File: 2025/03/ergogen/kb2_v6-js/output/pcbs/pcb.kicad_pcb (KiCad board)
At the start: 2 copper layers, 256 x 72 mm, 66 parts

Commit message: finish? keyboard
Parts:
- added _10: , Mount_Hole_2.2mm_Pad_Via, F.Cu at (235.0, 117.0)
- added _11: , Mount_Hole_2.2mm_Pad_Via, F.Cu at (181.0, 135.7)
- added _12: , Mount_Hole_2.2mm_Pad_Via, F.Cu at (253.0, 135.7)
- added _9: , Mount_Hole_2.2mm_Pad_Via, F.Cu at (254.0, 106.8)
- moved _4 145.8 mm to (180.0, 106.8)
- moved _3 72.8 mm to (180.5, 84.7)
- moved _6 68.0 mm to (325.0, 91.5)
- moved _8 55.5 mm to (252.5, 84.7)
- moved _7 50.9 mm to (235.0, 91.5)
- moved _5 27.0 mm to (199.0, 117.0)
- moved _2 18.0 mm to (199.0, 91.5)
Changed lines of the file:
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@@
         )
         (module "Mount_Hole_2.2mm_Pad_Via" (layer "F.Cu")
-          (at 181 91.5 0)
+          (at 199 91.5 0)
           (fp_text reference "_2" (at 0 -3.2) (layer "F.SilkS") hide
             (effects (font (size 1 1) (thickness 0.15)))
@@
         )
         (module "Mount_Hole_2.2mm_Pad_Via" (layer "F.Cu")
-          (at 253 91.5 0)
+          (at 180.5 84.7 0)
           (fp_text reference "_3" (at 0 -3.2) (layer "F.SilkS") hide
             (effects (font (size 1 1) (thickness 0.15)))
@@
         )
         (module "Mount_Hole_2.2mm_Pad_Via" (layer "F.Cu")
-          (at 325 91.5 0)
+          (at 180 106.8 0)
           (fp_text reference "_4" (at 0 -3.2) (layer "F.SilkS") hide
             (effects (font (size 1 1) (thickness 0.15)))
@@
         )
         (module "Mount_Hole_2.2mm_Pad_Via" (layer "F.Cu")
-          (at 172 117 0)
+          (at 199 117 0)
           (fp_text reference "_5" (at 0 -3.2) (layer "F.SilkS") hide
             (effects (font (size 1 1) (thickness 0.15)))
@@
         )
         (module "Mount_Hole_2.2mm_Pad_Via" (layer "F.Cu")
-          (at 262 117 0)
+          (at 325 91.5 0)
           (fp_text reference "_6" (at 0 -3.2) (layer "F.SilkS") hide
             (effects (font (size 1 1) (thickness 0.15)))
@@
         )
         (module "Mount_Hole_2.2mm_Pad_Via" (layer "F.Cu")
-          (at 207 134 0)
+          (at 235 91.5 0)
           (fp_text reference "_7" (at 0 -3.2) (layer "F.SilkS") hide
             (effects (font (size 1 1) (thickness 0.15)))
@@
         )
         (module "Mount_Hole_2.2mm_Pad_Via" (layer "F.Cu")
-          (at 227 134 0)
+          (at 252.5 84.7 0)
           (fp_text reference "_8" (at 0 -3.2) (layer "F.SilkS") hide
             (effects (font (size 1 1) (thickness 0.15)))
           )
+          (fp_circle (center 0 0) (end 2.45 0) (layer "F.CrtYd") (width 0.05) (fill none))
+          (pad "1" thru_hole circle locked (at 0 0) (size 4.4 4.4) (drill 2.2) (layers *.Cu *.Mask))
+          (pad "1" thru_hole circle locked (at 1.6296296296296298 0) (size 0.7 0.7) (drill 0.4) (layers *.Cu *.Mask))
+(pad "1" thru_hole circle locked (at 1.1523221619336332 1.152322161933633) (size 0.7 0.7) (drill 0.4) (layers *.Cu *.Mask))
+(pad "1" thru_hole circle locked (at 9.978603548608063e-17 1.6296296296296298) (size 0.7 0.7) (drill 0.4) (layers *.Cu *.Mask))
+(pad "1" thru_hole circle locked (at -1.152322161933633 1.1523221619336332) (size 0.7 0.7) (drill 0.4) (layers *.Cu *.Mask))
+(pad "1" thru_hole circle locked (at -1.6296296296296298 1.9957207097216127e-16) (size 0.7 0.7) (drill 0.4) (layers *.Cu *.Mask))
+(pad "1" thru_hole circle locked (at -1.1523221619336335 -1.152322161933633) (size 0.7 0.7) (drill 0.4) (layers *.Cu *.Mask))
+(pad "1" thru_hole circle locked (at -2.993581064582419e-16 -1.6296296296296298) (size 0.7 0.7) (drill 0.4) (layers *.Cu *.Mask))
+(pad "1" thru_hole circle locked (at 1.1523221619336328 -1.1523221619336335) (size 0.7 0.7) (drill 0.4) (layers *.Cu *.Mask))
+        )
+        (module "Mount_Hole_2.2mm_Pad_Via" (layer "F.Cu")
+          (at 254 106.8 0)
+          (fp_text reference "_9" (at 0 -3.2) (layer "F.SilkS") hide
+            (effects (font (size 1 1) (thickness 0.15)))
+          )
+          (fp_circle (center 0 0) (end 2.45 0) (layer "F.CrtYd") (width 0.05) (fill none))
+          (pad "1" thru_hole circle locked (at 0 0) (size 4.4 4.4) (drill 2.2) (layers *.Cu *.Mask))
+          (pad "1" thru_hole circle locked (at 1.6296296296296298 0) (size 0.7 0.7) (drill 0.4) (layers *.Cu *.Mask))
+(pad "1" thru_hole circle locked (at 1.1523221619336332 1.152322161933633) (size 0.7 0.7) (drill 0.4) (layers *.Cu *.Mask))
+(pad "1" thru_hole circle locked (at 9.978603548608063e-17 1.6296296296296298) (size 0.7 0.7) (drill 0.4) (layers *.Cu *.Mask))
+(pad "1" thru_hole circle locked (at -1.152322161933633 1.1523221619336332) (size 0.7 0.7) (drill 0.4) (layers *.Cu *.Mask))
+(pad "1" thru_hole circle locked (at -1.6296296296296298 1.9957207097216127e-16) (size 0.7 0.7) (drill 0.4) (layers *.Cu *.Mask))
+(pad "1" thru_hole circle locked (at -1.1523221619336335 -1.152322161933633) (size 0.7 0.7) (drill 0.4) (layers *.Cu *.Mask))
+(pad "1" thru_hole circle locked (at -2.993581064582419e-16 -1.6296296296296298) (size 0.7 0.7) (drill 0.4) (layers *.Cu *.Mask))
+(pad "1" thru_hole circle locked (at 1.1523221619336328 -1.1523221619336335) (size 0.7 0.7) (drill 0.4) (layers *.Cu *.Mask))
+        )
+        (module "Mount_Hole_2.2mm_Pad_Via" (layer "F.Cu")
+          (at 235 117 0)
+          (fp_text reference "_10" (at 0 -3.2) (layer "F.SilkS") hide
+            (effects (font (size 1 1) (thickness 0.15)))
+          )
+          (fp_circle (center 0 0) (end 2.45 0) (layer "F.CrtYd") (width 0.05) (fill none))
+          (pad "1" thru_hole circle locked (at 0 0) (size 4.4 4.4) (drill 2.2) (layers *.Cu *.Mask))
+          (pad "1" thru_hole circle locked (at 1.6296296296296298 0) (size 0.7 0.7) (drill 0.4) (layers *.Cu *.Mask))
+(pad "1" thru_hole circle locked (at 1.1523221619336332 1.152322161933633) (size 0.7 0.7) (drill 0.4) (layers *.Cu *.Mask))
+(pad "1" thru_hole circle locked (at 9.978603548608063e-17 1.6296296296296298) (size 0.7 0.7) (drill 0.4) (layers *.Cu *.Mask))
+(pad "1" thru_hole circle locked (at -1.152322161933633 1.1523221619336332) (size 0.7 0.7) (drill 0.4) (layers *.Cu *.Mask))
+(pad "1" thru_hole circle locked (at -1.6296296296296298 1.9957207097216127e-16) (size 0.7 0.7) (drill 0.4) (layers *.Cu *.Mask))
+(pad "1" thru_hole circle locked (at -1.1523221619336335 -1.152322161933633) (size 0.7 0.7) (drill 0.4) (layers *.Cu *.Mask))
+(pad "1" thru_hole circle locked (at -2.993581064582419e-16 -1.6296296296296298) (size 0.7 0.7) (drill 0.4) (layers *.Cu *.Mask))
+(pad "1" thru_hole circle locked (at 1.1523221619336328 -1.1523221619336335) (size 0.7 0.7) (drill 0.4) (layers *.Cu *.Mask))
+        )
+        (module "Mount_Hole_2.2mm_Pad_Via" (layer "F.Cu")
+          (at 181 135.7 0)
+          (fp_text reference "_11" (at 0 -3.2) (layer "F.SilkS") hide
+            (effects (font (size 1 1) (thickness 0.15)))
+          )
+          (fp_circle (center 0 0) (end 2.45 0) (layer "F.CrtYd") (width 0.05) (fill none))
+          (pad "1" thru_hole circle locked (at 0 0) (size 4.4 4.4) (drill 2.2) (layers *.Cu *.Mask))
+          (pad "1" thru_hole circle locked (at 1.6296296296296298 0) (size 0.7 0.7) (drill 0.4) (layers *.Cu *.Mask))
+(pad "1" thru_hole circle locked (at 1.1523221619336332 1.152322161933633) (size 0.7 0.7) (drill 0.4) (layers *.Cu *.Mask))
+(pad "1" thru_hole circle locked (at 9.978603548608063e-17 1.6296296296296298) (size 0.7 0.7) (drill 0.4) (layers *.Cu *.Mask))
+(pad "1" thru_hole circle locked (at -1.152322161933633 1.1523221619336332) (size 0.7 0.7) (drill 0.4) (layers *.Cu *.Mask))
+(pad "1" thru_hole circle locked (at -1.6296296296296298 1.9957207097216127e-16) (size 0.7 0.7) (drill 0.4) (layers *.Cu *.Mask))
+(pad "1" thru_hole circle locked (at -1.1523221619336335 -1.152322161933633) (size 0.7 0.7) (drill 0.4) (layers *.Cu *.Mask))
+(pad "1" thru_hole circle locked (at -2.993581064582419e-16 -1.6296296296296298) (size 0.7 0.7) (drill 0.4) (layers *.Cu *.Mask))
+(pad "1" thru_hole circle locked (at 1.1523221619336328 -1.1523221619336335) (size 0.7 0.7) (drill 0.4) (layers *.Cu *.Mask))
+        )
+        (module "Mount_Hole_2.2mm_Pad_Via" (layer "F.Cu")
+          (at 253 135.7 0)
+          (fp_text reference "_12" (at 0 -3.2) (layer "F.SilkS") hide
+            (effects (font (size 1 1) (thickness 0.15)))
+          )

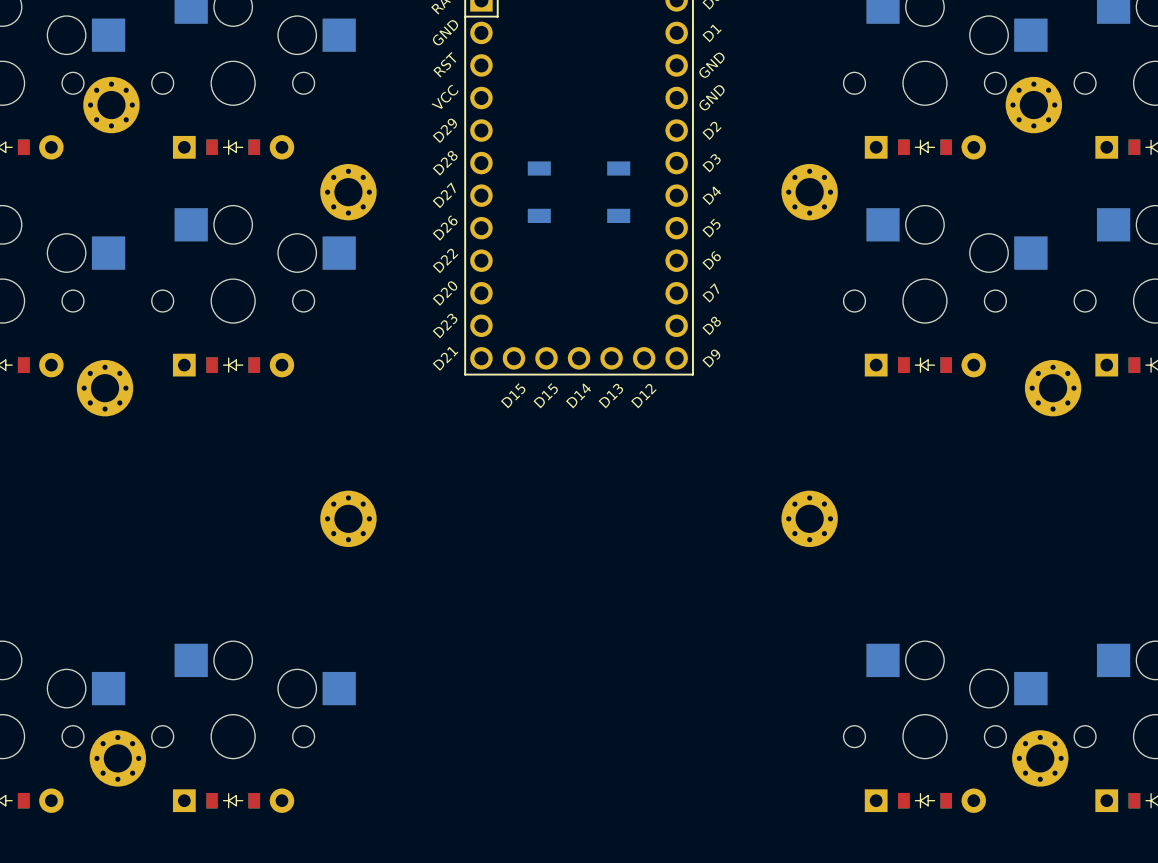
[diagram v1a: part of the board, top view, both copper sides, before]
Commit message: move screw holes to not interfere with switches
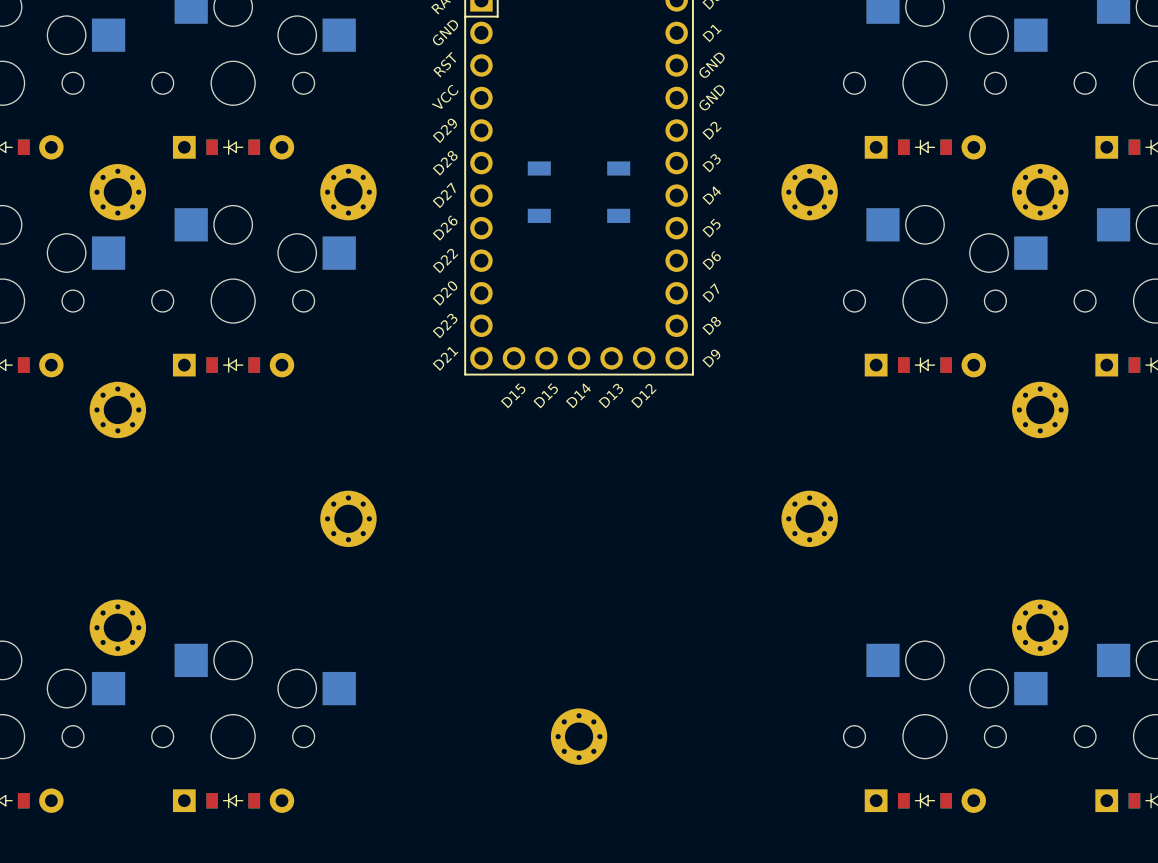
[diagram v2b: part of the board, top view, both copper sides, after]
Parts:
- added _13: , Mount_Hole_2.2mm_Pad_Via, F.Cu at (217.0, 134.0)
- moved _6 148.0 mm to (181.0, 125.5)
- moved _7 90.0 mm to (325.0, 91.5)
- moved _11 57.1 mm to (235.0, 117.0)
- moved _10 25.5 mm to (235.0, 91.5)
- moved _4 24.4 mm to (199.0, 91.5)
- moved _3 23.8 mm to (181.0, 108.5)
- moved _2 18.0 mm to (181.0, 91.5)
- moved _12 10.2 mm to (253.0, 125.5)
- moved _8 6.82 mm to (253.0, 91.5)
- moved _9 1.97 mm to (253.0, 108.5)
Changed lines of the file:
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@@
         )
         (module "Mount_Hole_2.2mm_Pad_Via" (layer "F.Cu")
-          (at 199 91.5 0)
+          (at 181 91.5 0)
           (fp_text reference "_2" (at 0 -3.2) (layer "F.SilkS") hide
             (effects (font (size 1 1) (thickness 0.15)))
@@
         )
         (module "Mount_Hole_2.2mm_Pad_Via" (layer "F.Cu")
-          (at 180.5 84.7 0)
+          (at 181 108.5 0)
           (fp_text reference "_3" (at 0 -3.2) (layer "F.SilkS") hide
             (effects (font (size 1 1) (thickness 0.15)))
@@
         )
         (module "Mount_Hole_2.2mm_Pad_Via" (layer "F.Cu")
-          (at 180 106.8 0)
+          (at 199 91.5 0)
           (fp_text reference "_4" (at 0 -3.2) (layer "F.SilkS") hide
             (effects (font (size 1 1) (thickness 0.15)))
@@
         )
         (module "Mount_Hole_2.2mm_Pad_Via" (layer "F.Cu")
-          (at 325 91.5 0)
+          (at 181 125.5 0)
           (fp_text reference "_6" (at 0 -3.2) (layer "F.SilkS") hide
             (effects (font (size 1 1) (thickness 0.15)))
@@
         )
         (module "Mount_Hole_2.2mm_Pad_Via" (layer "F.Cu")
-          (at 235 91.5 0)
+          (at 325 91.5 0)
           (fp_text reference "_7" (at 0 -3.2) (layer "F.SilkS") hide
             (effects (font (size 1 1) (thickness 0.15)))
@@
         )
         (module "Mount_Hole_2.2mm_Pad_Via" (layer "F.Cu")
-          (at 252.5 84.7 0)
+          (at 253 91.5 0)
           (fp_text reference "_8" (at 0 -3.2) (layer "F.SilkS") hide
             (effects (font (size 1 1) (thickness 0.15)))
@@
         )
         (module "Mount_Hole_2.2mm_Pad_Via" (layer "F.Cu")
-          (at 254 106.8 0)
+          (at 253 108.5 0)
           (fp_text reference "_9" (at 0 -3.2) (layer "F.SilkS") hide
             (effects (font (size 1 1) (thickness 0.15)))
@@
         )
         (module "Mount_Hole_2.2mm_Pad_Via" (layer "F.Cu")
-          (at 235 117 0)
+          (at 235 91.5 0)
           (fp_text reference "_10" (at 0 -3.2) (layer "F.SilkS") hide
             (effects (font (size 1 1) (thickness 0.15)))
@@
         )
         (module "Mount_Hole_2.2mm_Pad_Via" (layer "F.Cu")
-          (at 181 135.7 0)
+          (at 235 117 0)
           (fp_text reference "_11" (at 0 -3.2) (layer "F.SilkS") hide
             (effects (font (size 1 1) (thickness 0.15)))
@@
         )
         (module "Mount_Hole_2.2mm_Pad_Via" (layer "F.Cu")
-          (at 253 135.7 0)
+          (at 253 125.5 0)
           (fp_text reference "_12" (at 0 -3.2) (layer "F.SilkS") hide
             (effects (font (size 1 1) (thickness 0.15)))
           )
+          (fp_circle (center 0 0) (end 2.45 0) (layer "F.CrtYd") (width 0.05) (fill none))
+          (pad "1" thru_hole circle locked (at 0 0) (size 4.4 4.4) (drill 2.2) (layers *.Cu *.Mask))
+          (pad "1" thru_hole circle locked (at 1.6296296296296298 0) (size 0.7 0.7) (drill 0.4) (layers *.Cu *.Mask))
+(pad "1" thru_hole circle locked (at 1.1523221619336332 1.152322161933633) (size 0.7 0.7) (drill 0.4) (layers *.Cu *.Mask))
+(pad "1" thru_hole circle locked (at 9.978603548608063e-17 1.6296296296296298) (size 0.7 0.7) (drill 0.4) (layers *.Cu *.Mask))
+(pad "1" thru_hole circle locked (at -1.152322161933633 1.1523221619336332) (size 0.7 0.7) (drill 0.4) (layers *.Cu *.Mask))
+(pad "1" thru_hole circle locked (at -1.6296296296296298 1.9957207097216127e-16) (size 0.7 0.7) (drill 0.4) (layers *.Cu *.Mask))
+(pad "1" thru_hole circle locked (at -1.1523221619336335 -1.152322161933633) (size 0.7 0.7) (drill 0.4) (layers *.Cu *.Mask))
+(pad "1" thru_hole circle locked (at -2.993581064582419e-16 -1.6296296296296298) (size 0.7 0.7) (drill 0.4) (layers *.Cu *.Mask))
+(pad "1" thru_hole circle locked (at 1.1523221619336328 -1.1523221619336335) (size 0.7 0.7) (drill 0.4) (layers *.Cu *.Mask))
+        )
+        (module "Mount_Hole_2.2mm_Pad_Via" (layer "F.Cu")
+          (at 217 134 0)
+          (fp_text reference "_13" (at 0 -3.2) (layer "F.SilkS") hide
+            (effects (font (size 1 1) (thickness 0.15)))
+          )
